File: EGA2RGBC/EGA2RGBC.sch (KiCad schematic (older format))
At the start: 23 parts, among them J1 EGA Input, J2 CGA/EGA Selection, J3 CSync Selection, J4 Power, J5 Video Out, U1 74LS244, U2 74LS138, U3 74LS86

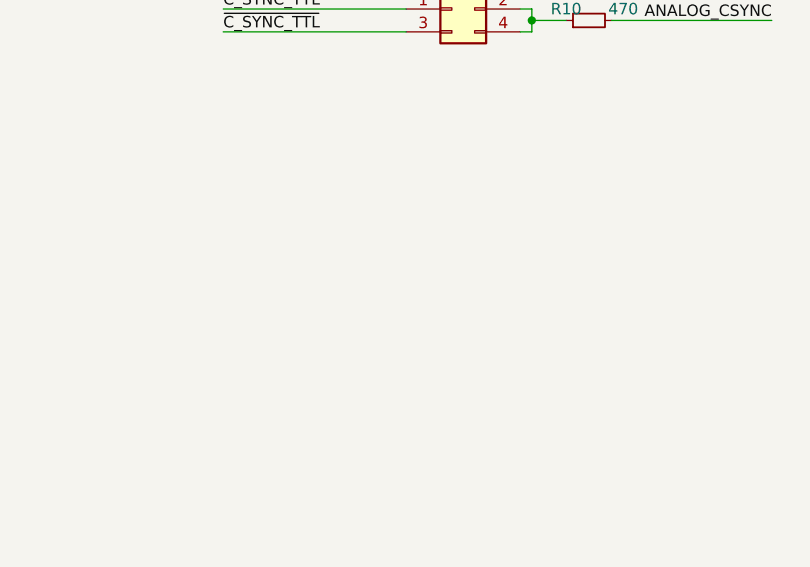
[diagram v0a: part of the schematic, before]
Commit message: Added footprints
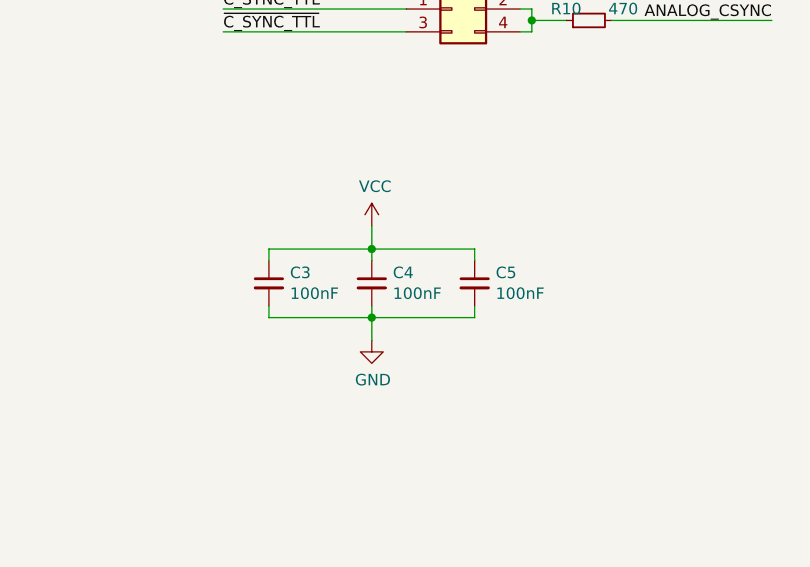
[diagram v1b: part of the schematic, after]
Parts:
- added C3, C4, C5: 100nF, Capacitor_THT:C_Disc_D6.0mm_W2.5mm_P5.00mm, symbol Device:C_Small
- C1, C2: footprint (none) -> Capacitor_THT:CP_Radial_D6.3mm_P2.50mm
- F1: footprint (none) -> Fuse:Fuse_1206_3216Metric
- J1: footprint (none) -> Connector_Dsub:DSUB-9_Female_Horizontal_P2.77x2.84mm_EdgePinOffset4.94mm_Housed_MountingHolesOffset7.48mm
- J2: footprint (none) -> Connector_PinHeader_2.54mm:PinHeader_2x04_P2.54mm_Vertical
- J3: footprint (none) -> Connector_PinHeader_2.54mm:PinHeader_2x02_P2.54mm_Vertical
- J4: footprint (none) -> TerminalBlock:TerminalBlock_bornier-2_P5.08mm
- J5: footprint (none) -> TerminalBlock:TerminalBlock_bornier-6_P5.08mm
- JP1: footprint (none) -> Connector_PinHeader_2.54mm:PinHeader_1x02_P2.54mm_Vertical
- R1, R10, R2, R3, R4, R5, R6, R7, R8, R9: footprint (none) -> Resistor_THT:R_Axial_DIN0204_L3.6mm_D1.6mm_P7.62mm_Horizontal
- U1: footprint (none) -> Package_DIP:DIP-20_W7.62mm
- U2: footprint (none) -> Package_DIP:DIP-16_W7.62mm
- U3: footprint (none) -> Package_DIP:DIP-14_W7.62mm
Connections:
- net GND: now also C3.2, C4.2, C5.2
- net VCC: now also C3.1, C4.1, C5.1
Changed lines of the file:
@@
 F 0 "J1" H 10530 1352 50  0000 L CNN
 F 1 "EGA Input" H 10530 1261 50  0000 L CNN
-F 2 "" H 10350 1350 50  0001 C CNN
+F 2 "Connector_Dsub:DSUB-9_Female_Horizontal_P2.77x2.84mm_EdgePinOffset4.94mm_Housed_MountingHolesOffset7.48mm" H 10350 1350 50  0001 C CNN
 F 3 " ~" H 10350 1350 50  0001 C CNN
 	1    10350 1350
@@
 F 0 "U1" H 2000 2400 50  0000 C CNN
 F 1 "74LS244" H 2500 2400 50  0000 C CNN
-F 2 "" H 2250 1750 50  0001 C CNN
+F 2 "Package_DIP:DIP-20_W7.62mm" H 2250 1750 50  0001 C CNN
 F 3 "http://www.ti.com/lit/ds/symlink/sn74ls244.pdf" H 2250 1750 50  0001 C CNN
 	1    2250 1750
@@
 F 0 "U3" H 4580 1646 50  0000 L CNN
 F 1 "74LS86" H 4580 1555 50  0000 L CNN
-F 2 "" H 4350 1600 50  0001 C CNN
+F 2 "Package_DIP:DIP-14_W7.62mm" H 4350 1600 50  0001 C CNN
 F 3 "74xx/74ls86.pdf" H 4350 1600 50  0001 C CNN
 	5    4350 1600
@@
 F 0 "U2" H 1850 5700 50  0000 C CNN
 F 1 "74LS138" H 2350 5700 50  0000 C CNN
-F 2 "" H 2150 5250 50  0001 C CNN
+F 2 "Package_DIP:DIP-16_W7.62mm" H 2150 5250 50  0001 C CNN
 F 3 "http://www.ti.com/lit/gpn/sn74LS138" H 2150 5250 50  0001 C CNN
 	1    2150 5250
@@
 F 0 "J2" H 2150 7167 50  0000 C CNN
 F 1 "CGA/EGA Selection" H 2150 7076 50  0000 C CNN
-F 2 "" H 2100 6850 50  0001 C CNN
+F 2 "Connector_PinHeader_2.54mm:PinHeader_2x04_P2.54mm_Vertical" H 2100 6850 50  0001 C CNN
 F 3 "~" H 2100 6850 50  0001 C CNN
 	1    2100 6850
@@
 F 0 "JP1" H 3250 6135 50  0000 C CNN
 F 1 "C128 Color Fix" H 3250 6044 50  0000 C CNN
-F 2 "" H 3250 5950 50  0001 C CNN
+F 2 "Connector_PinHeader_2.54mm:PinHeader_1x02_P2.54mm_Vertical" H 3250 5950 50  0001 C CNN
 F 3 "~" H 3250 5950 50  0001 C CNN
 	1    3250 5950
@@
 F 0 "R1" V 3300 5750 50  0000 C CNN
 F 1 "2k" V 3300 5500 50  0000 C CNN
-F 2 "" H 3250 5650 50  0001 C CNN
+F 2 "Resistor_THT:R_Axial_DIN0204_L3.6mm_D1.6mm_P7.62mm_Horizontal" H 3250 5650 50  0001 C CNN
 F 3 "~" H 3250 5650 50  0001 C CNN
 	1    3250 5650
@@
 F 0 "R2" V 2200 3350 50  0000 C CNN
 F 1 "470" V 2200 3100 50  0000 C CNN
-F 2 "" H 2150 3250 50  0001 C CNN
+F 2 "Resistor_THT:R_Axial_DIN0204_L3.6mm_D1.6mm_P7.62mm_Horizontal" H 2150 3250 50  0001 C CNN
 F 3 "~" H 2150 3250 50  0001 C CNN
 	1    2150 3250
@@
 F 0 "R3" V 2200 3500 50  0000 C CNN
 F 1 "1.5k" V 2200 3250 50  0000 C CNN
-F 2 "" H 2150 3400 50  0001 C CNN
+F 2 "Resistor_THT:R_Axial_DIN0204_L3.6mm_D1.6mm_P7.62mm_Horizontal" H 2150 3400 50  0001 C CNN
 F 3 "~" H 2150 3400 50  0001 C CNN
 	1    2150 3400
@@
 F 0 "R4" V 2200 3700 50  0000 C CNN
 F 1 "470" V 2200 3450 50  0000 C CNN
-F 2 "" H 2150 3600 50  0001 C CNN
+F 2 "Resistor_THT:R_Axial_DIN0204_L3.6mm_D1.6mm_P7.62mm_Horizontal" H 2150 3600 50  0001 C CNN
 F 3 "~" H 2150 3600 50  0001 C CNN
 	1    2150 3600
@@
 F 0 "R5" V 2200 3850 50  0000 C CNN
 F 1 "1.5k" V 2200 3600 50  0000 C CNN
-F 2 "" H 2150 3750 50  0001 C CNN
+F 2 "Resistor_THT:R_Axial_DIN0204_L3.6mm_D1.6mm_P7.62mm_Horizontal" H 2150 3750 50  0001 C CNN
 F 3 "~" H 2150 3750 50  0001 C CNN
 	1    2150 3750
@@
 F 0 "R6" V 2200 4050 50  0000 C CNN
 F 1 "470" V 2200 3800 50  0000 C CNN
-F 2 "" H 2150 3950 50  0001 C CNN
+F 2 "Resistor_THT:R_Axial_DIN0204_L3.6mm_D1.6mm_P7.62mm_Horizontal" H 2150 3950 50  0001 C CNN
 F 3 "~" H 2150 3950 50  0001 C CNN
 	1    2150 3950
@@
 F 0 "R7" V 2200 4200 50  0000 C CNN
 F 1 "1.5k" V 2200 3950 50  0000 C CNN
-F 2 "" H 2150 4100 50  0001 C CNN
+F 2 "Resistor_THT:R_Axial_DIN0204_L3.6mm_D1.6mm_P7.62mm_Horizontal" H 2150 4100 50  0001 C CNN
 F 3 "~" H 2150 4100 50  0001 C CNN
 	1    2150 4100
@@
 F 0 "U3" H 6900 1275 50  0000 C CNN
 F 1 "74LS86" H 6900 1184 50  0000 C CNN
-F 2 "" H 6900 950 50  0001 C CNN
+F 2 "Package_DIP:DIP-14_W7.62mm" H 6900 950 50  0001 C CNN
 F 3 "74xx/74ls86.pdf" H 6900 950 50  0001 C CNN
 	1    6900 950
@@
 F 0 "U3" H 6900 1925 50  0000 C CNN
 F 1 "74LS86" H 6900 1834 50  0000 C CNN
-F 2 "" H 6900 1600 50  0001 C CNN
+F 2 "Package_DIP:DIP-14_W7.62mm" H 6900 1600 50  0001 C CNN
 F 3 "74xx/74ls86.pdf" H 6900 1600 50  0001 C CNN
 	2    6900 1600
@@
 F 0 "U3" H 7800 1575 50  0000 C CNN
 F 1 "74LS86" H 7800 1484 50  0000 C CNN
-F 2 "" H 7800 1250 50  0001 C CNN
+F 2 "Package_DIP:DIP-14_W7.62mm" H 7800 1250 50  0001 C CNN
 F 3 "74xx/74ls86.pdf" H 7800 1250 50  0001 C CNN
 	3    7800 1250
@@
 F 0 "R8" V 6050 1150 50  0000 C CNN
 F 1 "10k" V 6050 900 50  0000 C CNN
-F 2 "" H 6000 1050 50  0001 C CNN
+F 2 "Resistor_THT:R_Axial_DIN0204_L3.6mm_D1.6mm_P7.62mm_Horizontal" H 6000 1050 50  0001 C CNN
 F 3 "~" H 6000 1050 50  0001 C CNN
 	1    6000 1050
@@
 F 0 "R9" V 6050 1800 50  0000 C CNN
 F 1 "10k" V 6050 1550 50  0000 C CNN
-F 2 "" H 6000 1700 50  0001 C CNN
+F 2 "Resistor_THT:R_Axial_DIN0204_L3.6mm_D1.6mm_P7.62mm_Horizontal" H 6000 1700 50  0001 C CNN
 F 3 "~" H 6000 1700 50  0001 C CNN
 	1    6000 1700
@@
 F 0 "C1" H 6391 1196 50  0000 L CNN
 F 1 "1uF" H 6391 1105 50  0000 L CNN
-F 2 "" H 6300 1150 50  0001 C CNN
+F 2 "Capacitor_THT:CP_Radial_D6.3mm_P2.50mm" H 6300 1150 50  0001 C CNN
 F 3 "~" H 6300 1150 50  0001 C CNN
 	1    6300 1150
@@
 F 0 "C2" H 6391 1846 50  0000 L CNN
 F 1 "1uF" H 6391 1755 50  0000 L CNN
-F 2 "" H 6300 1800 50  0001 C CNN
+F 2 "Capacitor_THT:CP_Radial_D6.3mm_P2.50mm" H 6300 1800 50  0001 C CNN
 F 3 "~" H 6300 1800 50  0001 C CNN
 	1    6300 1800
@@
 F 0 "U3" H 6900 2775 50  0000 C CNN
 F 1 "74LS86" H 6900 2684 50  0000 C CNN
-F 2 "" H 6900 2450 50  0001 C CNN
+F 2 "Package_DIP:DIP-14_W7.62mm" H 6900 2450 50  0001 C CNN
 F 3 "74xx/74ls86.pdf" H 6900 2450 50  0001 C CNN
 	4    6900 2450
@@
 F 0 "J3" H 6900 3267 50  0000 C CNN
 F 1 "CSync Selection" H 6900 3176 50  0000 C CNN
-F 2 "" H 6850 3050 50  0001 C CNN
+F 2 "Connector_PinHeader_2.54mm:PinHeader_2x02_P2.54mm_Vertical" H 6850 3050 50  0001 C CNN
 F 3 "~" H 6850 3050 50  0001 C CNN
 	1    6850 3050
@@
 F 0 "R10" V 7500 3200 50  0000 C CNN
 F 1 "470" V 7500 2950 50  0000 C CNN
-F 2 "" H 7450 3100 50  0001 C CNN
+F 2 "Resistor_THT:R_Axial_DIN0204_L3.6mm_D1.6mm_P7.62mm_Horizontal" H 7450 3100 50  0001 C CNN
 F 3 "~" H 7450 3100 50  0001 C CNN
 	1    7450 3100
@@
 F 0 "J4" H 10222 3024 50  0000 R CNN
 F 1 "Power" H 10222 2933 50  0000 R CNN
-F 2 "" H 10250 3050 50  0001 C CNN
+F 2 "TerminalBlock:TerminalBlock_bornier-2_P5.08mm" H 10250 3050 50  0001 C CNN
 F 3 "~" H 10250 3050 50  0001 C CNN
 	1    10250 3050
@@
 F 0 "F1" H 9700 3235 50  0000 C CNN
 F 1 "250mA" H 9700 3144 50  0000 C CNN
-F 2 "" H 9700 3050 50  0001 C CNN
+F 2 "Fuse:Fuse_1206_3216Metric" H 9700 3050 50  0001 C CNN
 F 3 "~" H 9700 3050 50  0001 C CNN
 	1    9700 3050
@@
 F 0 "J5" H 10330 4292 50  0000 L CNN
 F 1 "Video Out" H 10330 4201 50  0000 L CNN
-F 2 "" H 10250 4300 50  0001 C CNN
+F 2 "TerminalBlock:TerminalBlock_bornier-6_P5.08mm" H 10250 4300 50  0001 C CNN
 F 3 "~" H 10250 4300 50  0001 C CNN
 	1    10250 4300
@@
 	9350 4500 9350 4600
 Connection ~ 9350 4600
+$Comp
+L Device:C_Small C3
+U 1 1 5FE76EBB
+P 6050 4250
+F 0 "C3" H 6142 4296 50  0000 L CNN
+F 1 "100nF" H 6142 4205 50  0000 L CNN
+F 2 "Capacitor_THT:C_Disc_D6.0mm_W2.5mm_P5.00mm" H 6050 4250 50  0001 C CNN
+F 3 "~" H 6050 4250 50  0001 C CNN
+	1    6050 4250
+	1    0    0    -1
+$EndComp
+$Comp
+L Device:C_Small C4
+U 1 1 5FE787A6
+P 6500 4250
+F 0 "C4" H 6592 4296 50  0000 L CNN
+F 1 "100nF" H 6592 4205 50  0000 L CNN
+F 2 "Capacitor_THT:C_Disc_D6.0mm_W2.5mm_P5.00mm" H 6500 4250 50  0001 C CNN
+F 3 "~" H 6500 4250 50  0001 C CNN
+	1    6500 4250
+	1    0    0    -1
+$EndComp
+$Comp
+L Device:C_Small C5
+U 1 1 5FE79134
+P 6950 4250
+F 0 "C5" H 7042 4296 50  0000 L CNN
+F 1 "100nF" H 7042 4205 50  0000 L CNN
+F 2 "Capacitor_THT:C_Disc_D6.0mm_W2.5mm_P5.00mm" H 6950 4250 50  0001 C CNN
+F 3 "~" H 6950 4250 50  0001 C CNN
+	1    6950 4250
+	1    0    0    -1
+$EndComp
+Wire Wire Line
+	6050 4150 6050 4100
+Wire Wire Line
+	6050 4100 6500 4100
+Wire Wire Line
+	6950 4100 6950 4150
+Wire Wire Line
+	6500 4150 6500 4100
+Connection ~ 6500 4100
+Wire Wire Line
+	6500 4100 6950 4100
+Wire Wire Line
+	6050 4350 6050 4400
+Wire Wire Line
+	6050 4400 6500 4400
+Wire Wire Line
+	6950 4400 6950 4350
+Wire Wire Line
+	6500 4350 6500 4400
+Connection ~ 6500 4400
+Wire Wire Line
+	6500 4400 6950 4400
+$Comp
+L power:GND #PWR?
+U 1 1 5FE94DFF
+P 6500 4500
+F 0 "#PWR?" H 6500 4250 50  0001 C CNN
+F 1 "GND" H 6505 4327 50  0000 C CNN
+F 2 "" H 6500 4500 50  0001 C CNN
+F 3 "" H 6500 4500 50  0001 C CNN
+	1    6500 4500
+	1    0    0    -1
+$EndComp
+Wire Wire Line
+	6500 4400 6500 4500
+$Comp
+L power:VCC #PWR?
+U 1 1 5FEA8753
+P 6500 4000
+F 0 "#PWR?" H 6500 3850 50  0001 C CNN
+F 1 "VCC" H 6515 4173 50  0000 C CNN
+F 2 "" H 6500 4000 50  0001 C CNN
+F 3 "" H 6500 4000 50  0001 C CNN
+	1    6500 4000
+	1    0    0    -1
+$EndComp
+Wire Wire Line
+	6500 4000 6500 4100
 $EndSCHEMATC

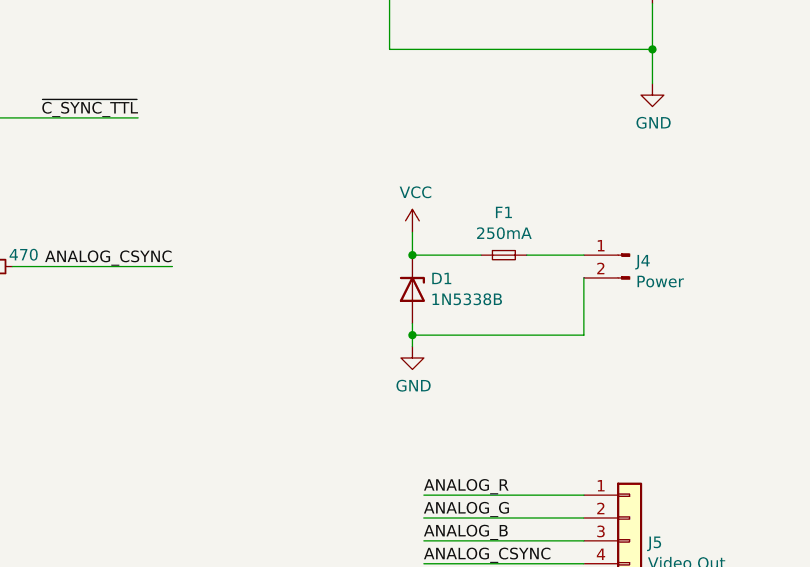
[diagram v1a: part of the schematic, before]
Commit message: Fix labels and generate gerbers
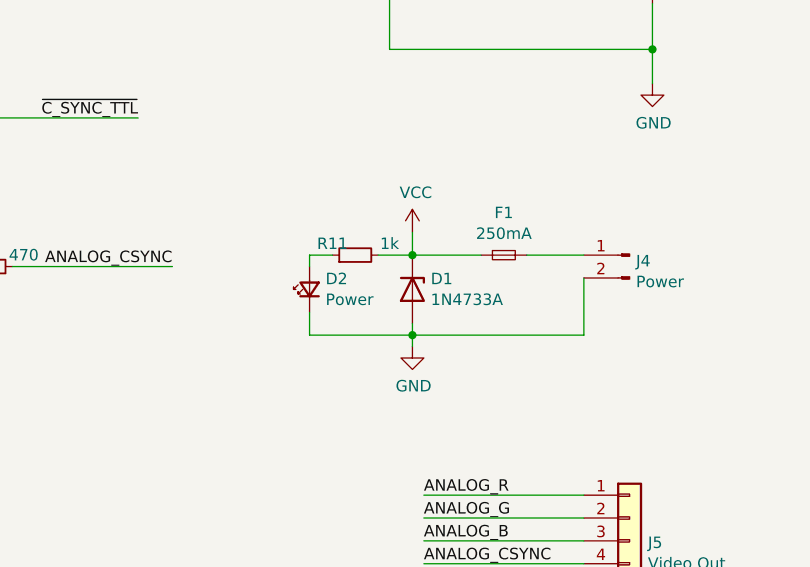
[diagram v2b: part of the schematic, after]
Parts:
- removed D1: 1N5338B, Diode_THT:D_DO-201_P15.24mm_Horizontal, symbol Diode:1N53xxB
- added D1: 1N4733A, Diode_THT:D_DO-41_SOD81_P10.16mm_Horizontal, symbol Diode:1N47xxA
- added D2: Power, LED_THT:LED_D2.0mm_W4.8mm_H2.5mm_FlatTop, symbol Device:LED_Small
- added R11: 1k, Resistor_THT:R_Axial_DIN0204_L3.6mm_D1.6mm_P7.62mm_Horizontal, symbol Device:R_Small
- C1, C2: footprint Capacitor_THT:CP_Radial_D6.3mm_P2.50mm -> Capacitor_THT:CP_Radial_D5.0mm_P2.50mm
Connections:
- net GND: now also D1.2 (A), D2.1 (K)
- net VCC: now also D1.1 (K), R11.2
- new net: D2.2 (A), R11.1
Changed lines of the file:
@@
 	1500 2200 1500 2250
 $Comp
-L power:GND #PWR?
+L power:GND #PWR0101
 U 1 1 5FC01F63
 P 2250 2850
-F 0 "#PWR?" H 2250 2600 50  0001 C CNN
+F 0 "#PWR0101" H 2250 2600 50  0001 C CNN
 F 1 "GND" H 2255 2677 50  0000 C CNN
 F 2 "" H 2250 2850 50  0001 C CNN
@@
 Connection ~ 2250 2700
 $Comp
-L power:VCC #PWR?
+L power:VCC #PWR0102
 U 1 1 5FC0338F
 P 2250 800
-F 0 "#PWR?" H 2250 650 50  0001 C CNN
+F 0 "#PWR0102" H 2250 650 50  0001 C CNN
 F 1 "VCC" H 2265 973 50  0000 C CNN
 F 2 "" H 2250 800 50  0001 C CNN
@@
 BUF_G
 $Comp
-L power:VCC #PWR?
+L power:VCC #PWR0103
 U 1 1 5FC29BA0
 P 2150 4500
-F 0 "#PWR?" H 2150 4350 50  0001 C CNN
+F 0 "#PWR0103" H 2150 4350 50  0001 C CNN
 F 1 "VCC" H 2165 4673 50  0000 C CNN
 F 2 "" H 2150 4500 50  0001 C CNN
@@
 	2150 4600 2150 4650
 $Comp
-L power:GND #PWR?
+L power:GND #PWR0104
 U 1 1 5FC34069
 P 2150 6100
-F 0 "#PWR?" H 2150 5850 50  0001 C CNN
+F 0 "#PWR0104" H 2150 5850 50  0001 C CNN
 F 1 "GND" H 2155 5927 50  0000 C CNN
 F 2 "" H 2150 6100 50  0001 C CNN
@@
 ANALOG_B
 $Comp
-L power:VCC #PWR?
+L power:VCC #PWR0105
 U 1 1 5FCAE014
 P 4350 950
-F 0 "#PWR?" H 4350 800 50  0001 C CNN
+F 0 "#PWR0105" H 4350 800 50  0001 C CNN
 F 1 "VCC" H 4365 1123 50  0000 C CNN
 F 2 "" H 4350 950 50  0001 C CNN
@@
 	4350 950  4350 1100
 $Comp
-L power:GND #PWR?
+L power:GND #PWR0106
 U 1 1 5FCB5164
 P 4350 2250
-F 0 "#PWR?" H 4350 2000 50  0001 C CNN
+F 0 "#PWR0106" H 4350 2000 50  0001 C CNN
 F 1 "GND" H 4355 2077 50  0000 C CNN
 F 2 "" H 4350 2250 50  0001 C CNN
@@
 F 0 "C1" H 6391 1196 50  0000 L CNN
 F 1 "1uF" H 6391 1105 50  0000 L CNN
-F 2 "Capacitor_THT:CP_Radial_D6.3mm_P2.50mm" H 6300 1150 50  0001 C CNN
+F 2 "Capacitor_THT:CP_Radial_D5.0mm_P2.50mm" H 6300 1150 50  0001 C CNN
 F 3 "~" H 6300 1150 50  0001 C CNN
 	1    6300 1150
@@
 F 0 "C2" H 6391 1846 50  0000 L CNN
 F 1 "1uF" H 6391 1755 50  0000 L CNN
-F 2 "Capacitor_THT:CP_Radial_D6.3mm_P2.50mm" H 6300 1800 50  0001 C CNN
+F 2 "Capacitor_THT:CP_Radial_D5.0mm_P2.50mm" H 6300 1800 50  0001 C CNN
 F 3 "~" H 6300 1800 50  0001 C CNN
 	1    6300 1800
@@
 	6300 1700 6600 1700
 $Comp
-L power:GND #PWR?
+L power:GND #PWR0107
 U 1 1 5FCF157C
 P 6300 1300
-F 0 "#PWR?" H 6300 1050 50  0001 C CNN
+F 0 "#PWR0107" H 6300 1050 50  0001 C CNN
 F 1 "GND" H 6150 1250 50  0000 C CNN
 F 2 "" H 6300 1300 50  0001 C CNN
@@
 	6300 1250 6300 1300
 $Comp
-L power:GND #PWR?
+L power:GND #PWR0108
 U 1 1 5FCFBCB6
 P 6300 1950
-F 0 "#PWR?" H 6300 1700 50  0001 C CNN
+F 0 "#PWR0108" H 6300 1700 50  0001 C CNN
 F 1 "GND" H 6150 1900 50  0000 C CNN
 F 2 "" H 6300 1950 50  0001 C CNN
@@
 	6600 2550 5850 2550
 $Comp
-L power:VCC #PWR?
+L power:VCC #PWR0109
 U 1 1 5FD1F304
 P 5850 2200
-F 0 "#PWR?" H 5850 2050 50  0001 C CNN
+F 0 "#PWR0109" H 5850 2050 50  0001 C CNN
 F 1 "VCC" H 5865 2373 50  0000 C CNN
 F 2 "" H 5850 2200 50  0001 C CNN
@@
 Connection ~ 10350 2150
 $Comp
-L power:GND #PWR?
+L power:GND #PWR0110
 U 1 1 5FD62624
 P 10350 2300
-F 0 "#PWR?" H 10350 2050 50  0001 C CNN
+F 0 "#PWR0110" H 10350 2050 50  0001 C CNN
 F 1 "GND" H 10355 2127 50  0000 C CNN
 F 2 "" H 10350 2300 50  0001 C CNN
@@
 $EndComp
 $Comp
-L power:GND #PWR?
+L power:GND #PWR0111
 U 1 1 5FDC0023
 P 9300 3450
-F 0 "#PWR?" H 9300 3200 50  0001 C CNN
+F 0 "#PWR0111" H 9300 3200 50  0001 C CNN
 F 1 "GND" H 9305 3277 50  0000 C CNN
 F 2 "" H 9300 3450 50  0001 C CNN
@@
 	1    9300 3450
 	1    0    0    -1
-$EndComp
-$Comp
-L Diode:1N53xxB D1
-U 1 1 5FDC92F9
-P 9300 3200
-F 0 "D1" V 9254 3280 50  0000 L CNN
-F 1 "1N5338B" V 9345 3280 50  0000 L CNN
-F 2 "Diode_THT:D_DO-201_P15.24mm_Horizontal" H 9300 3025 50  0001 C CNN
-F 3 "https://diotec.com/tl_files/diotec/files/pdf/datasheets/1n5345b.pdf" H 9300 3200 50  0001 C CNN
-	1    9300 3200
-	0    1    1    0
 $EndComp
 Wire Wire Line
@@
 	9600 3050 9300 3050
 $Comp
-L power:VCC #PWR?
+L power:VCC #PWR0112
 U 1 1 5FDFFBDD
 P 9300 2950
-F 0 "#PWR?" H 9300 2800 50  0001 C CNN
+F 0 "#PWR0112" H 9300 2800 50  0001 C CNN
 F 1 "VCC" H 9315 3123 50  0000 C CNN
 F 2 "" H 9300 2950 50  0001 C CNN
@@
 Wire Wire Line
 	9300 2950 9300 3050
-Connection ~ 9300 3050
 Wire Wire Line
 	10050 4100 9350 4100
@@
 	10050 4600 9350 4600
 $Comp
-L power:GND #PWR?
+L power:GND #PWR0113
 U 1 1 5FE2A2FA
 P 9350 4700
-F 0 "#PWR?" H 9350 4450 50  0001 C CNN
+F 0 "#PWR0113" H 9350 4450 50  0001 C CNN
 F 1 "GND" H 9355 4527 50  0000 C CNN
 F 2 "" H 9350 4700 50  0001 C CNN
@@
 	6500 4400 6950 4400
 $Comp
-L power:GND #PWR?
+L power:GND #PWR0114
 U 1 1 5FE94DFF
 P 6500 4500
-F 0 "#PWR?" H 6500 4250 50  0001 C CNN
+F 0 "#PWR0114" H 6500 4250 50  0001 C CNN
 F 1 "GND" H 6505 4327 50  0000 C CNN
 F 2 "" H 6500 4500 50  0001 C CNN
@@
 	6500 4400 6500 4500
 $Comp
-L power:VCC #PWR?
+L power:VCC #PWR0115
 U 1 1 5FEA8753
 P 6500 4000
-F 0 "#PWR?" H 6500 3850 50  0001 C CNN
+F 0 "#PWR0115" H 6500 3850 50  0001 C CNN
 F 1 "VCC" H 6515 4173 50  0000 C CNN
 F 2 "" H 6500 4000 50  0001 C CNN
@@
 Wire Wire Line
 	6500 4000 6500 4100
+$Comp
+L Diode:1N47xxA D1
+U 1 1 5FEF2862
+P 9300 3200
+F 0 "D1" V 9254 3280 50  0000 L CNN
+F 1 "1N4733A" V 9345 3280 50  0000 L CNN
+F 2 "Diode_THT:D_DO-41_SOD81_P10.16mm_Horizontal" H 9300 3025 50  0001 C CNN
+F 3 "https://www.vishay.com/docs/85816/1n4728a.pdf" H 9300 3200 50  0001 C CNN
+	1    9300 3200
+	0    1    1    0
+$EndComp
+Connection ~ 9300 3050
+$Comp
+L Device:LED_Small D2
+U 1 1 5FF05BD7
+P 8850 3200
+F 0 "D2" V 8896 3130 50  0000 R CNN
+F 1 "Power" V 8805 3130 50  0000 R CNN
+F 2 "LED_THT:LED_D2.0mm_W4.8mm_H2.5mm_FlatTop" V 8850 3200 50  0001 C CNN
+F 3 "~" V 8850 3200 50  0001 C CNN
+	1    8850 3200
+	0    -1   -1   0
+$EndComp
+Wire Wire Line
+	8850 3300 8850 3400
+Wire Wire Line
+	8850 3400 9300 3400
+$Comp
+L Device:R_Small R11
+U 1 1 5FF43F49
+P 9050 3050
+F 0 "R11" V 9100 3150 50  0000 C CNN
+F 1 "1k" V 9100 2900 50  0000 C CNN
+F 2 "Resistor_THT:R_Axial_DIN0204_L3.6mm_D1.6mm_P7.62mm_Horizontal" H 9050 3050 50  0001 C CNN
+F 3 "~" H 9050 3050 50  0001 C CNN
+	1    9050 3050
+	0    -1   -1   0
+$EndComp
+Wire Wire Line
+	9150 3050 9300 3050
+Wire Wire Line
+	8950 3050 8850 3050
+Wire Wire Line
+	8850 3050 8850 3100
 $EndSCHEMATC
